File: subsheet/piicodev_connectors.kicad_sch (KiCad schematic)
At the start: 4 parts, among them J1501 Conn_01x04, J1502 Conn_01x04, U1501 D1213A-04TS-7

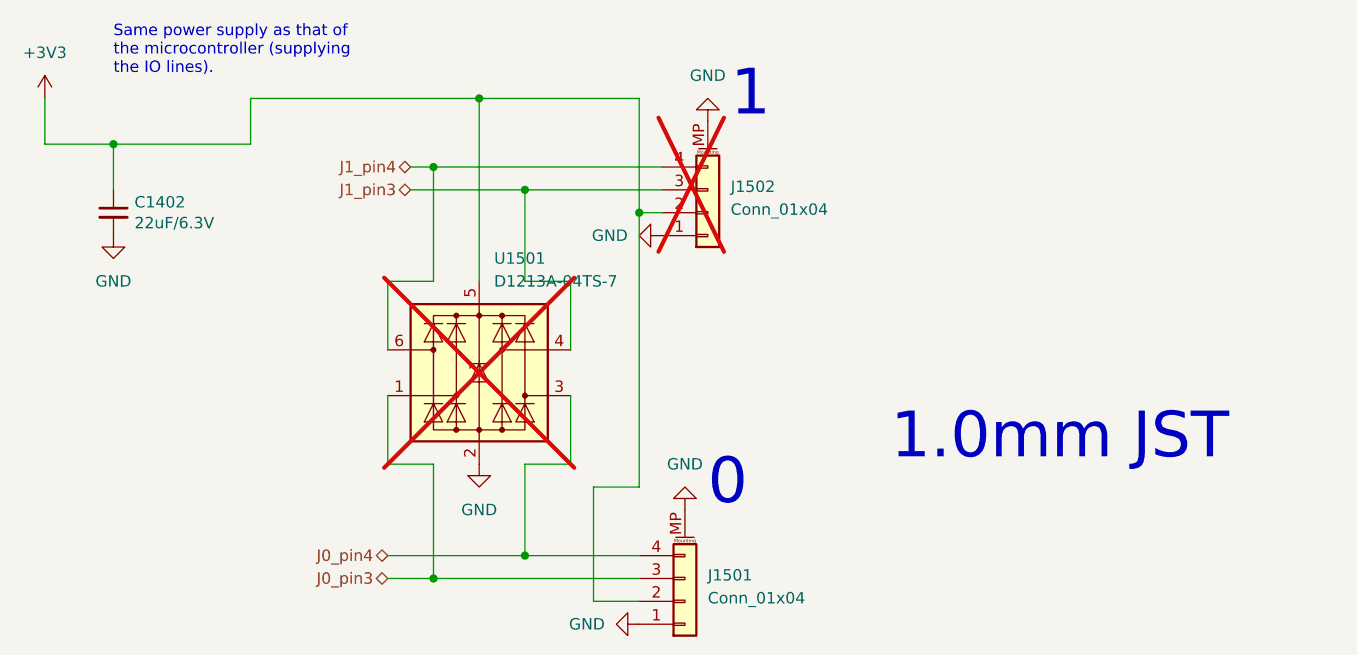
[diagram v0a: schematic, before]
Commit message: Move all subsheets into 'main' subsheet, below root
Keeping all the subsheets in a dedicated 'subsheet' folder makes things
much, much neater. However, specifying filepaths for subsheets has an
interesting problem; they use paths RELATIVE TO THE PARENT SHEET.

The consequence of is that if a subsheet is part of the root sheet, it
needs to be prefixed with 'subsheet/', but NOT if it's further down.
This inconsistency can be resolved by having a single 'main' sheet at
the top that doesn't move.

It's also useful to have a top-level space to put down changelogs,
descriptions etc.
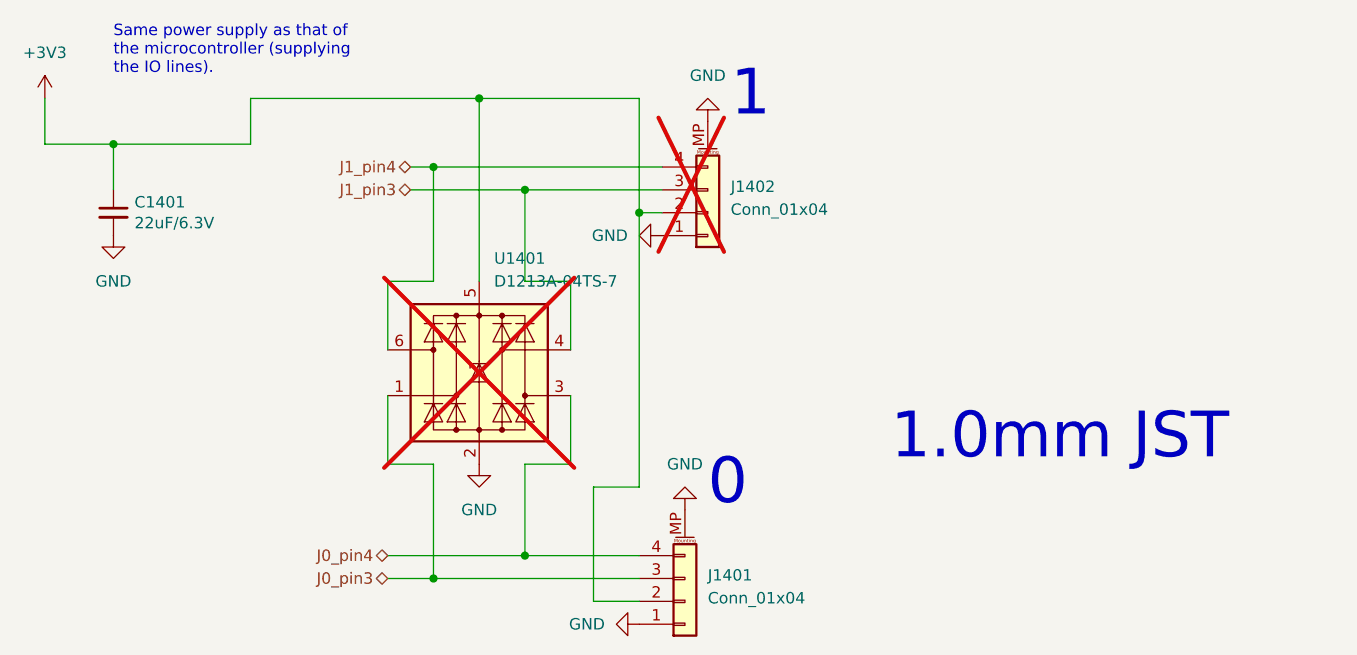
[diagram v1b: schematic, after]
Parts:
- renumbered C1402 to C1401, J1501 to J1401, J1502 to J1402, U1501 to U1401
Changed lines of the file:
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@@
 		(shape bidirectional)
 		(at 68.58 109.22 180)
-		(fields_autoplaced yes)
 		(effects
 			(font
@@
 		(shape bidirectional)
 		(at 66.04 154.94 180)
-		(fields_autoplaced yes)
 		(effects
 			(font
@@
 		(shape bidirectional)
 		(at 68.58 111.76 180)
-		(fields_autoplaced yes)
 		(effects
 			(font
@@
 		(shape bidirectional)
 		(at 66.04 152.4 180)
-		(fields_autoplaced yes)
 		(effects
 			(font
@@
 		(dnp no)
 		(fields_autoplaced yes)
-		(property "Reference" "#PWR01506"
+		(property "Reference" "#PWR1407"
 			(at 101.6 97.79 0)
 			(effects
@@
 		(instances
 			(project "ESP_bare_chip_test_board"
-				(path "/45b6f84a-e69b-48be-a49b-bc68872e2c15/04b60eee-d553-4abe-8b22-3fc74b6351bd"
-					(reference "#PWR01506")
+				(path "/45b6f84a-e69b-48be-a49b-bc68872e2c15/f48098a1-cacc-4192-b650-2a34a2ba76dc/2fa57716-ed63-4f9e-9bb4-1ad832d9ecf9"
+					(reference "#PWR1407")
 					(unit 1)
 				)
@@
 		(on_board yes)
 		(dnp no)
-		(property "Reference" "C1402"
+		(property "Reference" "C1401"
 			(at 37.8968 113.1316 0)
 			(effects
@@
 		(instances
 			(project "ESP_bare_chip_test_board"
-				(path "/45b6f84a-e69b-48be-a49b-bc68872e2c15/04b60eee-d553-4abe-8b22-3fc74b6351bd"
-					(reference "C1402")
+				(path "/45b6f84a-e69b-48be-a49b-bc68872e2c15/f48098a1-cacc-4192-b650-2a34a2ba76dc/2fa57716-ed63-4f9e-9bb4-1ad832d9ecf9"
+					(reference "C1401")
 					(unit 1)
 				)
@@
 		(dnp no)
 		(fields_autoplaced yes)
-		(property "Reference" "J1501"
+		(property "Reference" "J1401"
 			(at 101.6 154.5844 0)
 			(effects
@@
 		(instances
 			(project "ESP_bare_chip_test_board"
-				(path "/45b6f84a-e69b-48be-a49b-bc68872e2c15/04b60eee-d553-4abe-8b22-3fc74b6351bd"
-					(reference "J1501")
+				(path "/45b6f84a-e69b-48be-a49b-bc68872e2c15/f48098a1-cacc-4192-b650-2a34a2ba76dc/2fa57716-ed63-4f9e-9bb4-1ad832d9ecf9"
+					(reference "J1401")
 					(unit 1)
 				)
@@
 		(dnp no)
 		(fields_autoplaced yes)
-		(property "Reference" "#PWR01501"
+		(property "Reference" "#PWR1401"
 			(at 27.94 105.41 0)
 			(effects
@@
 		(instances
 			(project "ESP_bare_chip_test_board"
-				(path "/45b6f84a-e69b-48be-a49b-bc68872e2c15/04b60eee-d553-4abe-8b22-3fc74b6351bd"
-					(reference "#PWR01501")
+				(path "/45b6f84a-e69b-48be-a49b-bc68872e2c15/f48098a1-cacc-4192-b650-2a34a2ba76dc/2fa57716-ed63-4f9e-9bb4-1ad832d9ecf9"
+					(reference "#PWR1401")
 					(unit 1)
 				)
@@
 		(dnp no)
 		(fields_autoplaced yes)
-		(property "Reference" "#PWR01505"
+		(property "Reference" "#PWR1406"
 			(at 99.06 140.97 0)
 			(effects
@@
 		(instances
 			(project "ESP_bare_chip_test_board"
-				(path "/45b6f84a-e69b-48be-a49b-bc68872e2c15/04b60eee-d553-4abe-8b22-3fc74b6351bd"
-					(reference "#PWR01505")
+				(path "/45b6f84a-e69b-48be-a49b-bc68872e2c15/f48098a1-cacc-4192-b650-2a34a2ba76dc/2fa57716-ed63-4f9e-9bb4-1ad832d9ecf9"
+					(reference "#PWR1406")
 					(unit 1)
 				)
@@
 		(dnp no)
 		(fields_autoplaced yes)
-		(property "Reference" "#PWR01502"
+		(property "Reference" "#PWR1403"
 			(at 76.2 148.59 0)
 			(effects
@@
 		(instances
 			(project "ESP_bare_chip_test_board"
-				(path "/45b6f84a-e69b-48be-a49b-bc68872e2c15/04b60eee-d553-4abe-8b22-3fc74b6351bd"
-					(reference "#PWR01502")
+				(path "/45b6f84a-e69b-48be-a49b-bc68872e2c15/f48098a1-cacc-4192-b650-2a34a2ba76dc/2fa57716-ed63-4f9e-9bb4-1ad832d9ecf9"
+					(reference "#PWR1403")
 					(unit 1)
 				)
@@
 		(on_board yes)
 		(dnp no)
-		(property "Reference" "#PWR01503"
+		(property "Reference" "#PWR1404"
 			(at 87.63 160.02 0)
 			(effects
@@
 		(instances
 			(project "ESP_bare_chip_test_board"
-				(path "/45b6f84a-e69b-48be-a49b-bc68872e2c15/04b60eee-d553-4abe-8b22-3fc74b6351bd"
-					(reference "#PWR01503")
+				(path "/45b6f84a-e69b-48be-a49b-bc68872e2c15/f48098a1-cacc-4192-b650-2a34a2ba76dc/2fa57716-ed63-4f9e-9bb4-1ad832d9ecf9"
+					(reference "#PWR1404")
 					(unit 1)
 				)
@@
 		(dnp yes)
 		(fields_autoplaced yes)
-		(property "Reference" "U1501"
+		(property "Reference" "U1401"
 			(at 77.8511 119.38 0)
 			(effects
@@
 		(instances
 			(project "ESP_bare_chip_test_board"
-				(path "/45b6f84a-e69b-48be-a49b-bc68872e2c15/04b60eee-d553-4abe-8b22-3fc74b6351bd"
-					(reference "U1501")
+				(path "/45b6f84a-e69b-48be-a49b-bc68872e2c15/f48098a1-cacc-4192-b650-2a34a2ba76dc/2fa57716-ed63-4f9e-9bb4-1ad832d9ecf9"
+					(reference "U1401")
 					(unit 1)
 				)
@@
 		(dnp yes)
 		(fields_autoplaced yes)
-		(property "Reference" "J1502"
+		(property "Reference" "J1402"
 			(at 104.14 111.4044 0)
 			(effects
@@
 		(instances
 			(project "ESP_bare_chip_test_board"
-				(path "/45b6f84a-e69b-48be-a49b-bc68872e2c15/04b60eee-d553-4abe-8b22-3fc74b6351bd"
-					(reference "J1502")
+				(path "/45b6f84a-e69b-48be-a49b-bc68872e2c15/f48098a1-cacc-4192-b650-2a34a2ba76dc/2fa57716-ed63-4f9e-9bb4-1ad832d9ecf9"
+					(reference "J1402")
 					(unit 1)
 				)
@@
 		(dnp no)
 		(fields_autoplaced yes)
-		(property "Reference" "#PWR01404"
+		(property "Reference" "#PWR1402"
 			(at 35.56 123.19 0)
 			(effects
@@
 		(instances
 			(project "ESP_bare_chip_test_board"
-				(path "/45b6f84a-e69b-48be-a49b-bc68872e2c15/04b60eee-d553-4abe-8b22-3fc74b6351bd"
-					(reference "#PWR01404")
+				(path "/45b6f84a-e69b-48be-a49b-bc68872e2c15/f48098a1-cacc-4192-b650-2a34a2ba76dc/2fa57716-ed63-4f9e-9bb4-1ad832d9ecf9"
+					(reference "#PWR1402")
 					(unit 1)
 				)
@@
 		(dnp no)
 		(fields_autoplaced yes)
-		(property "Reference" "#PWR01504"
+		(property "Reference" "#PWR1405"
 			(at 90.17 116.84 0)
 			(effects
@@
 		(instances
 			(project "ESP_bare_chip_test_board"
-				(path "/45b6f84a-e69b-48be-a49b-bc68872e2c15/04b60eee-d553-4abe-8b22-3fc74b6351bd"
-					(reference "#PWR01504")
-					(unit 1)
-				)
+				(path "/45b6f84a-e69b-48be-a49b-bc68872e2c15/f48098a1-cacc-4192-b650-2a34a2ba76dc/2fa57716-ed63-4f9e-9bb4-1ad832d9ecf9"
+					(reference "#PWR1405")
+					(unit 1)
+				)
